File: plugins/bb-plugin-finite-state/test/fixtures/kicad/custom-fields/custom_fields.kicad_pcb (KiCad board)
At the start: 2 copper layers, 30 x 22 mm, 2 parts, among them J1 Conn_01x02

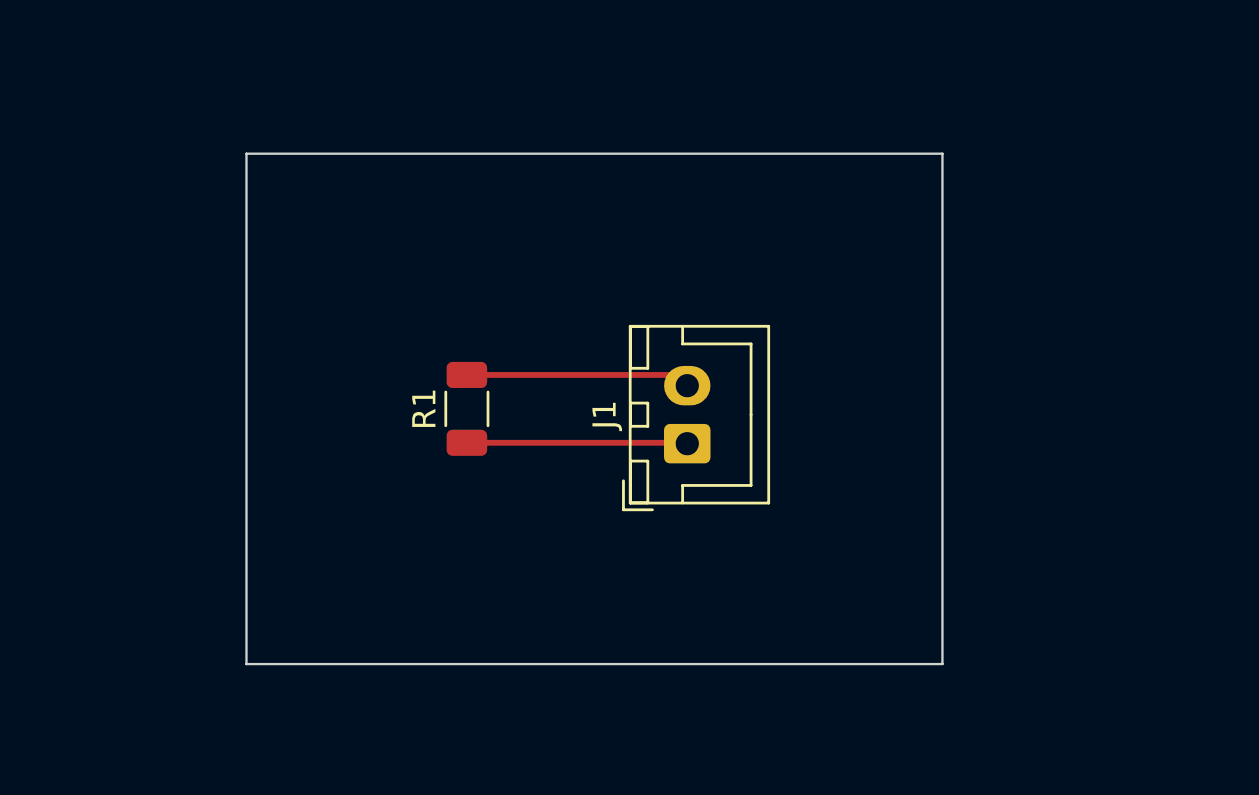
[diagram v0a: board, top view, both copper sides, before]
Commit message: fs plugin: replace GPL KiCad fixture
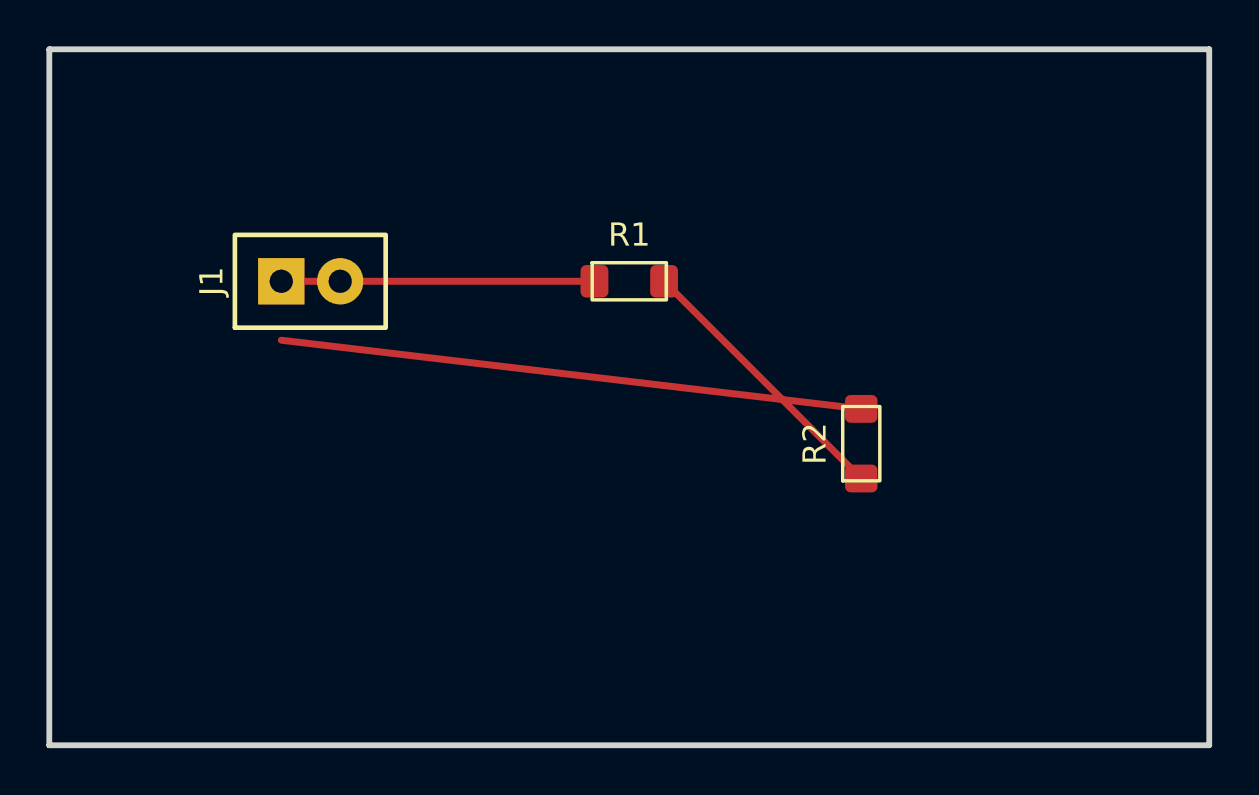
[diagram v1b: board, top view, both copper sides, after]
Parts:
- added R2: 47k, Fixture:R_0603, F.Cu at (60.0, 42.0)
- J1: value Conn_01x02 -> CONTROL_IN; footprint Connector_JST:JST_XH_B2B-XH-A_1x02_P2.50mm_Vertical -> Fixture:Header_1x02
- R1: value R -> 10k; footprint Resistor_SMD:R_1206_3216Metric -> Fixture:R_0603
- moved J1 18.8 mm to (35.0, 35.0)
- moved R1 8.90 mm to (50.0, 35.0), turned to 0 degrees
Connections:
- net Net-(J1-Pad1) renamed INPUT_SIGNAL
- J1 pad 2: Net-(J1-Pad2) -> RETURN_LINK
- R1 pad 2: Net-(J1-Pad2) -> CONTROL
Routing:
- net RETURN_LINK: track 0.00 -> 25.2 mm
- net CONTROL: track 0.00 -> 12.0 mm
- net Net-(J1-Pad2): track 9.69 -> 0.00 mm
- net INPUT_SIGNAL: track 9.52 -> 13.5 mm
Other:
- board size 30 x 22 mm -> 50 x 30 mm
